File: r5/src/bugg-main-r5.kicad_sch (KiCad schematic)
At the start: 43 parts, among them T14 , T15 , T16 , T3 , T39 , T40 , U1 74LVC1G07DCK, U34 74LVC1G157GV

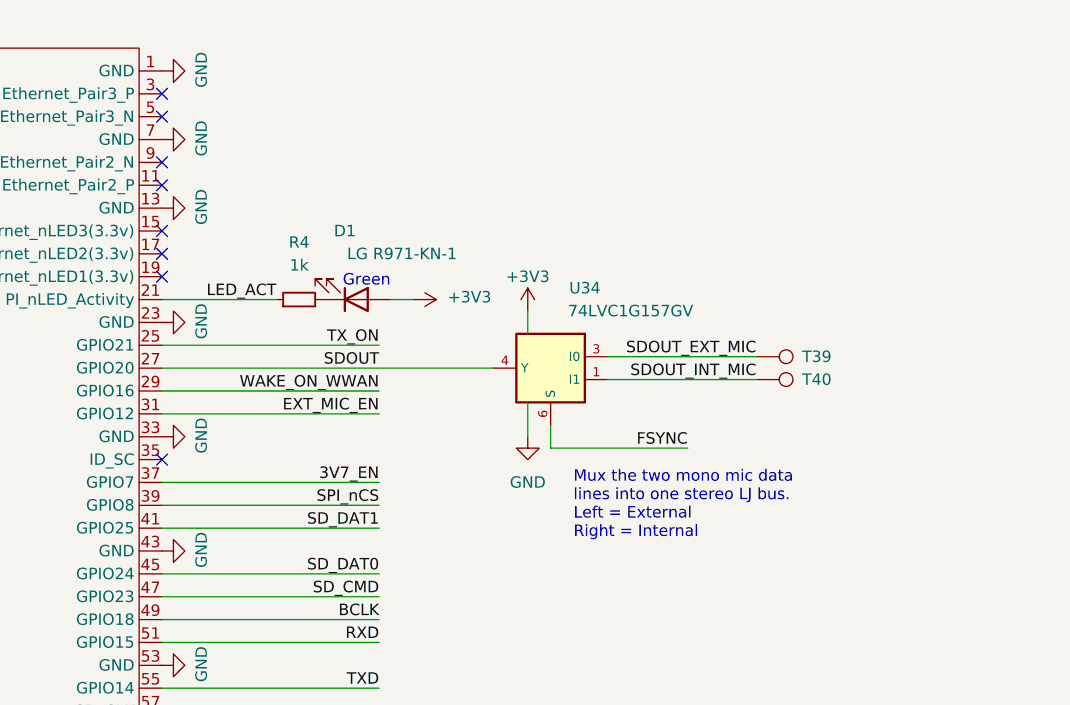
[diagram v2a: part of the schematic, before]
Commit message: Add missing decoupling cap to audio data mux
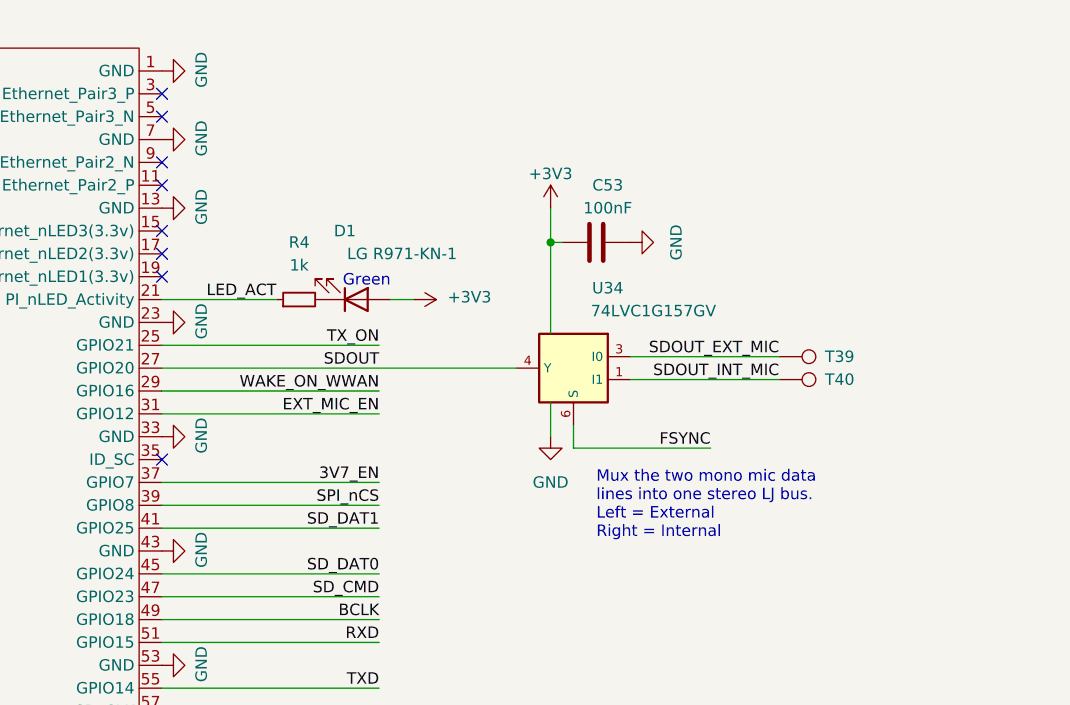
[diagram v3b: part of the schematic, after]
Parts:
- added C53: 100nF, Capacitor_SMD:C_0402_1005Metric, symbol Device:C
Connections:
- net +3V3: now also C53.2
- net GND: now also C53.1
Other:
- moved on the sheet: T39, T40, U34
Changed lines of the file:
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@@
   (junction (at 243.84 170.18) (diameter 1.016) (color 0 0 0 0)
   )
+  (junction (at 283.21 92.71) (diameter 0) (color 0 0 0 0)
+  )
   (junction (at 243.84 175.26) (diameter 1.016) (color 0 0 0 0)
   )
@@
     (stroke (width 0) (type solid))
   )
-  (wire (pts (xy 283.21 113.03) (xy 283.21 115.57))
+  (wire (pts (xy 285.75 113.03) (xy 285.75 115.57))
     (stroke (width 0) (type default))
   )
@@
     (stroke (width 0) (type solid))
   )
-  (wire (pts (xy 283.21 115.57) (xy 298.45 115.57))
+  (wire (pts (xy 285.75 115.57) (xy 300.99 115.57))
     (stroke (width 0) (type default))
   )
@@
     (stroke (width 0) (type solid))
   )
+  (wire (pts (xy 283.21 92.71) (xy 283.21 102.87))
+    (stroke (width 0) (type default))
+  )
   (wire (pts (xy 146.05 142.24) (xy 147.32 142.24))
     (stroke (width 0) (type solid))
@@
     (stroke (width 0) (type solid))
   )
-  (wire (pts (xy 280.67 110.49) (xy 280.67 114.3))
+  (wire (pts (xy 283.21 110.49) (xy 283.21 114.3))
     (stroke (width 0) (type default))
   )
@@
     (stroke (width 0) (type solid))
   )
-  (wire (pts (xy 289.56 105.41) (xy 306.07 105.41))
+  (wire (pts (xy 292.1 105.41) (xy 308.61 105.41))
+    (stroke (width 0) (type default))
+  )
+  (wire (pts (xy 283.21 92.71) (xy 284.48 92.71))
     (stroke (width 0) (type default))
   )
@@
     (stroke (width 0) (type solid))
   )
-  (wire (pts (xy 289.56 107.95) (xy 306.07 107.95))
+  (wire (pts (xy 292.1 107.95) (xy 308.61 107.95))
     (stroke (width 0) (type default))
   )
@@
     (stroke (width 0) (type solid))
   )
-  (wire (pts (xy 280.67 100.33) (xy 280.67 102.87))
+  (wire (pts (xy 283.21 88.9) (xy 283.21 92.71))
     (stroke (width 0) (type default))
   )
@@
     (stroke (width 0) (type solid))
   )
-  (wire (pts (xy 240.03 106.68) (xy 276.86 106.68))
+  (wire (pts (xy 240.03 106.68) (xy 279.4 106.68))
     (stroke (width 0) (type solid))
   )
@@
   )
   (text "Mux the two mono mic data \nlines into one stereo LJ bus.\nLeft = External\nRight = Internal" (exclude_from_sim no)
-    (at 285.75 125.73 0)
+    (at 288.29 125.73 0)
     (effects (font (size 1.27 1.27)) (justify left bottom))
   )
@@
     (effects (font (size 1.27 1.27)) (justify left bottom))
   )
-  (label "SDOUT_EXT_MIC" (at 306.07 105.41 180) (fields_autoplaced)
+  (label "SDOUT_EXT_MIC" (at 308.61 105.41 180) (fields_autoplaced)
     (effects (font (size 1.27 1.27)) (justify right bottom))
   )
@@
     (effects (font (size 1.27 1.27)) (justify left bottom))
   )
-  (label "SDOUT_INT_MIC" (at 306.07 107.95 180) (fields_autoplaced)
+  (label "SDOUT_INT_MIC" (at 308.61 107.95 180) (fields_autoplaced)
     (effects (font (size 1.27 1.27)) (justify right bottom))
   )
@@
     (effects (font (size 1.27 1.27)) (justify left bottom))
   )
-  (label "FSYNC" (at 298.45 115.57 180) (fields_autoplaced)
+  (label "FSYNC" (at 300.99 115.57 180) (fields_autoplaced)
     (effects (font (size 1.27 1.27)) (justify right bottom))
   )
@@
     )
   )
-  (symbol (lib_id "power:+3V3") (at 280.67 100.33 0) (unit 1)
+  (symbol (lib_id "power:+3V3") (at 283.21 88.9 0) (unit 1)
     (in_bom yes) (on_board yes) (dnp no)
-    (property "Reference" "#PWR037" (at 280.67 104.14 0)
+    (property "Reference" "#PWR037" (at 283.21 92.71 0)
       (effects (font (size 1.27 1.27)) hide)
     )
-    (property "Value" "+3V3" (at 280.67 96.52 0)
+    (property "Value" "+3V3" (at 283.21 85.09 0)
       (effects (font (size 1.27 1.27)))
     )
-    (property "Footprint" "" (at 280.67 100.33 0)
+    (property "Footprint" "" (at 283.21 88.9 0)
       (effects (font (size 1.27 1.27)) hide)
     )
-    (property "Datasheet" "" (at 280.67 100.33 0)
+    (property "Datasheet" "" (at 283.21 88.9 0)
       (effects (font (size 1.27 1.27)) hide)
     )
@@
     )
   )
-  (symbol (lib_id "Connector:TestPoint") (at 306.07 105.41 270) (unit 1)
+  (symbol (lib_id "Connector:TestPoint") (at 308.61 105.41 270) (unit 1)
     (in_bom yes) (on_board yes) (dnp no)
-    (property "Reference" "T39" (at 311.15 105.41 90)
+    (property "Reference" "T39" (at 313.69 105.41 90)
       (effects (font (size 1.27 1.27)) (justify left))
     )
-    (property "Value" " " (at 311.15 104.14 90)
+    (property "Value" " " (at 313.69 104.14 90)
       (effects (font (size 1.27 1.27)) (justify left))
     )
-    (property "Footprint" "TestPoint:TestPoint_Pad_D1.0mm" (at 306.07 110.49 0)
+    (property "Footprint" "TestPoint:TestPoint_Pad_D1.0mm" (at 308.61 110.49 0)
       (effects (font (size 1.27 1.27)) hide)
     )
-    (property "Datasheet" "~" (at 306.07 110.49 0)
+    (property "Datasheet" "~" (at 308.61 110.49 0)
       (effects (font (size 1.27 1.27)) hide)
     )
@@
     )
   )
-  (symbol (lib_id "j_74xGxx:74LVC1G157") (at 283.21 106.68 0) (mirror y) (unit 1)
+  (symbol (lib_id "j_74xGxx:74LVC1G157") (at 285.75 106.68 0) (mirror y) (unit 1)
     (in_bom yes) (on_board yes) (dnp no)
-    (property "Reference" "U34" (at 287.02 97.79 0)
+    (property "Reference" "U34" (at 289.56 97.79 0)
       (effects (font (size 1.27 1.27)))
     )
-    (property "Value" "74LVC1G157GV" (at 292.1 100.33 0)
+    (property "Value" "74LVC1G157GV" (at 294.64 100.33 0)
       (effects (font (size 1.27 1.27)))
     )
-    (property "Footprint" "Package_SO:SC-74-6_1.5x2.9mm_P0.95mm" (at 283.21 106.68 0)
+    (property "Footprint" "Package_SO:SC-74-6_1.5x2.9mm_P0.95mm" (at 285.75 106.68 0)
       (effects (font (size 1.27 1.27)) hide)
     )
-    (property "Datasheet" "" (at 283.21 106.68 0)
+    (property "Datasheet" "" (at 285.75 106.68 0)
       (effects (font (size 1.27 1.27)) hide)
     )
@@
     )
   )
-  (symbol (lib_id "power:GND") (at 280.67 114.3 0) (unit 1)
+  (symbol (lib_id "power:GND") (at 283.21 114.3 0) (unit 1)
     (in_bom yes) (on_board yes) (dnp no)
-    (property "Reference" "#PWR038" (at 280.67 120.65 0)
+    (property "Reference" "#PWR038" (at 283.21 120.65 0)
       (effects (font (size 1.27 1.27)) hide)
     )
-    (property "Value" "GND" (at 280.67 119.38 0)
+    (property "Value" "GND" (at 283.21 119.38 0)
       (effects (font (size 1.27 1.27)))
     )
-    (property "Footprint" "" (at 280.67 114.3 0)
+    (property "Footprint" "" (at 283.21 114.3 0)
       (effects (font (size 1.27 1.27)) hide)
     )
-    (property "Datasheet" "" (at 280.67 114.3 0)
+    (property "Datasheet" "" (at 283.21 114.3 0)
       (effects (font (size 1.27 1.27)) hide)
     )
@@
     )
   )
+  (symbol (lib_id "power:GND") (at 292.1 92.71 90) (unit 1)
+    (in_bom yes) (on_board yes) (dnp no)
+    (property "Reference" "#PWR0306" (at 298.45 92.71 0)
+      (effects (font (size 1.27 1.27)) hide)
+    )
+    (property "Value" "GND" (at 297.18 92.71 0)
+      (effects (font (size 1.27 1.27)))
+    )
+    (property "Footprint" "" (at 292.1 92.71 0)
+      (effects (font (size 1.27 1.27)) hide)
+    )
+    (property "Datasheet" "" (at 292.1 92.71 0)
+      (effects (font (size 1.27 1.27)) hide)
+    )
+    (pin "1")
+    (instances
+      (project "bugg-main-r5"
+        (path "/e3eb514f-6ce4-4abe-ba20-f82f0015628f"
+          (reference "#PWR0306") (unit 1)
+        )
+      )
+    )
+  )
   (symbol (lib_id "Device:R") (at 290.83 36.83 90) (unit 1)
     (in_bom yes) (on_board yes) (dnp no)
@@
     )
   )
-  (symbol (lib_id "Connector:TestPoint") (at 306.07 107.95 270) (unit 1)
+  (symbol (lib_id "Connector:TestPoint") (at 308.61 107.95 270) (unit 1)
     (in_bom yes) (on_board yes) (dnp no)
-    (property "Reference" "T40" (at 311.15 107.95 90)
+    (property "Reference" "T40" (at 313.69 107.95 90)
       (effects (font (size 1.27 1.27)) (justify left))
     )
-    (property "Value" " " (at 311.15 106.68 90)
+    (property "Value" " " (at 313.69 106.68 90)
       (effects (font (size 1.27 1.27)) (justify left))
     )
-    (property "Footprint" "TestPoint:TestPoint_Pad_D1.0mm" (at 306.07 113.03 0)
+    (property "Footprint" "TestPoint:TestPoint_Pad_D1.0mm" (at 308.61 113.03 0)
       (effects (font (size 1.27 1.27)) hide)
     )
-    (property "Datasheet" "~" (at 306.07 113.03 0)
+    (property "Datasheet" "~" (at 308.61 113.03 0)
       (effects (font (size 1.27 1.27)) hide)
     )
@@
         )
       )
+    )
+  )
+  (symbol (lib_id "Device:C") (at 288.29 92.71 270) (mirror x) (unit 1)
+    (in_bom yes) (on_board yes) (dnp no)
+    (property "Reference" "C53" (at 289.56 86.36 90)
+      (effects (font (size 1.27 1.27)))
+    )
+    (property "Value" "100nF" (at 289.56 88.9 90)
+      (effects (font (size 1.27 1.27)))
+    )
+    (property "Footprint" "Capacitor_SMD:C_0402_1005Metric" (at 284.48 91.7448 0)
+      (effects (font (size 1.27 1.27)) hide)
+    )
+    (property "Datasheet" "~" (at 288.29 92.71 0)
+      (effects (font (size 1.27 1.27)) hide)
+    )
+    (pin "1")
+    (pin "2")
+    (instances
+      (project "bugg-main-r5"
+        (path "/e3eb514f-6ce4-4abe-ba20-f82f0015628f/41f15edd-4583-4f5d-8a81-daeb7c83b416"
+          (reference "C53") (unit 1)
+        )
+        (path "/e3eb514f-6ce4-4abe-ba20-f82f0015628f"
+          (reference "C137") (unit 1)
+        )
+      )

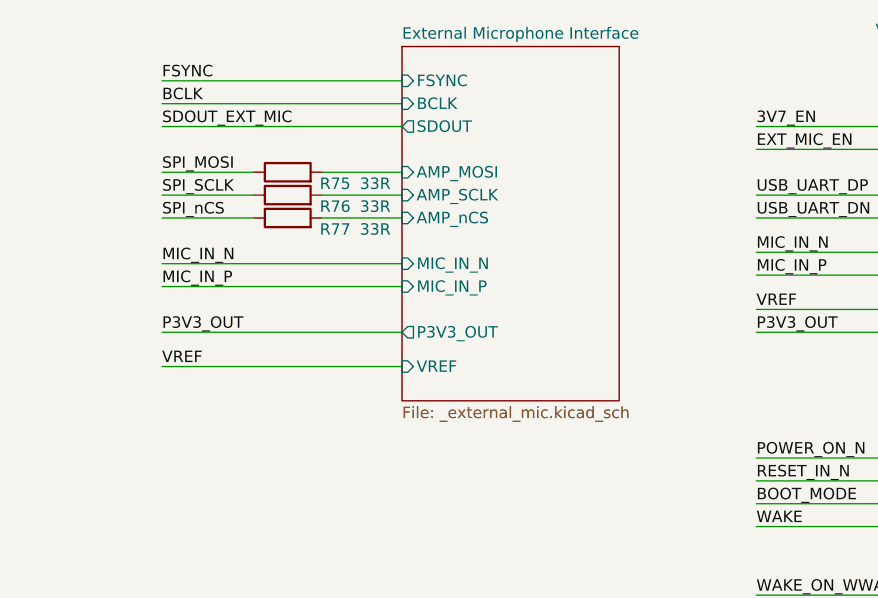
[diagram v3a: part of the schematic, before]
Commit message: Add voltage supervisor to detect 5V USB presence and force P3V3 phantom to be disabled even if it's selected
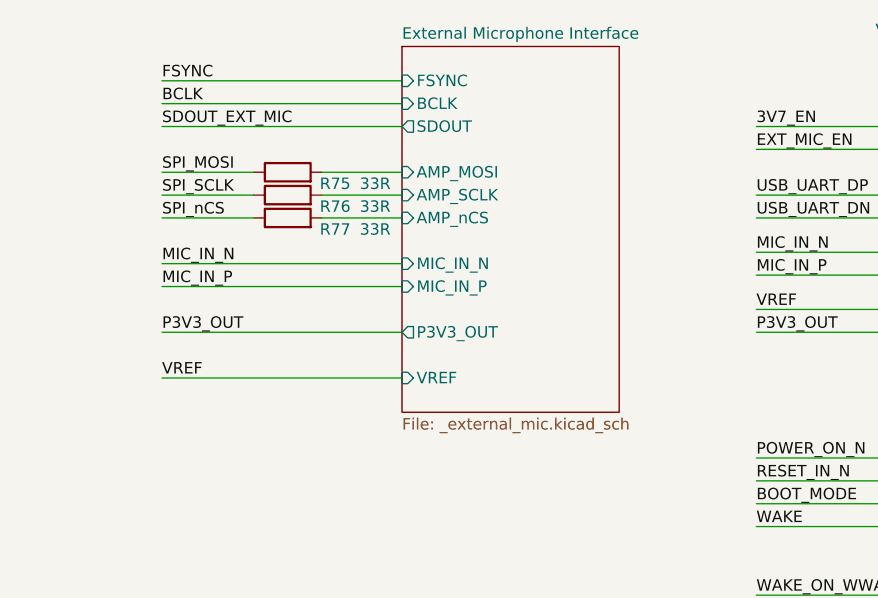
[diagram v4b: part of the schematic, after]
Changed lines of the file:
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@@
     (stroke (width 0) (type default))
   )
-  (wire (pts (xy 276.86 58.42) (xy 303.53 58.42))
+  (wire (pts (xy 276.86 59.69) (xy 303.53 59.69))
     (stroke (width 0) (type default))
   )
@@
     (effects (font (size 1.27 1.27)) (justify right bottom))
   )
-  (label "VREF" (at 276.86 58.42 0) (fields_autoplaced)
+  (label "VREF" (at 276.86 59.69 0) (fields_autoplaced)
     (effects (font (size 1.27 1.27)) (justify left bottom))
   )
@@
     )
   )
-  (sheet (at 303.53 22.86) (size 24.13 39.37) (fields_autoplaced)
+  (sheet (at 303.53 22.86) (size 24.13 40.64) (fields_autoplaced)
     (stroke (width 0.1524) (type solid) (color 132 0 132 1))
     (fill (color 255 255 255 0.0000))
@@
       (effects (font (size 1.27 1.27)) (justify left bottom))
     )
-    (property "Sheetfile" "_external_mic.kicad_sch" (at 303.53 62.8146 0)
+    (property "Sheetfile" "_external_mic.kicad_sch" (at 303.53 64.0846 0)
       (effects (font (size 1.27 1.27)) (justify left top))
     )
@@
       (effects (font (size 1.27 1.27)) (justify left))
     )
-    (pin "VREF" input (at 303.53 58.42 180)
-      (effects (font (size 1.27 1.27)) (justify left))
-    )
+    (pin "VREF" input (at 303.53 59.69 180)
+      (effects (font (size 1.27 1.27)) (justify left))
+    )
